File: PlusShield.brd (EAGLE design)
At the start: 79.7 x 67.3 mm, 32 parts, among them K1 G6J-2P-Y, K2 G6J-2P-Y

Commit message: Added PNGs and gnd vias.
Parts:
- added U$4, U$5: (no value), Robin:SAFECAST_LOGO
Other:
- board text added: "License CC-BY-SA 3.0"
- board text added: "PlusShield v1.0"
- board text added: "SAFECAST Japan"
- board text added: "by Robin Scheibler and Joe Moross"
- board text added: "https://github.com/Safecast/PlusShield"
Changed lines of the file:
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@@
 <text x="56.642" y="9.652" size="0.762" layer="21" rot="R90">5V</text>
 <text x="56.896" y="5.334" size="0.762" layer="21" rot="R180">PULSE</text>
+<text x="2.54" y="63.5" size="1.778" layer="21">PlusShield v1.0</text>
+<text x="26.67" y="64.77" size="0.762" layer="21">by Robin Scheibler and Joe Moross</text>
+<text x="26.67" y="63.5" size="0.762" layer="21">License CC-BY-SA 3.0</text>
+<text x="26.67" y="62.23" size="0.762" layer="21">https://github.com/Safecast/PlusShield</text>
+<text x="2.54" y="60.96" size="1.778" layer="21">SAFECAST Japan</text>
 </plain>
 <attributes>
@@
 <element name="C2" library="SparkFun" package="CAP-PTH-5MM" value="0.1uF" x="70.5358" y="54.0512" rot="R90"/>
 <element name="USB2" library="SparkFun" package="1X04" value="" x="77.47" y="11.43" smashed="yes" rot="R90">
-<attribute name="NAME" x="77.9272" y="21.0058" size="1.27" layer="25" ratio="10" rot="R90"/>
 <attribute name="VALUE" x="80.645" y="10.16" size="1.27" layer="27" rot="R90"/>
 </element>
 <element name="USB1" library="SparkFun" package="1X04" value="" x="64.77" y="2.54" smashed="yes" rot="R90">
-<attribute name="NAME" x="65.2272" y="12.1158" size="1.27" layer="25" ratio="10" rot="R90"/>
 <attribute name="VALUE" x="67.945" y="1.27" size="1.27" layer="27" rot="R90"/>
 </element>
@@
 </element>
 <element name="SIG1" library="SparkFun" package="1X04" value="" x="58.42" y="2.54" smashed="yes" rot="R90">
-<attribute name="NAME" x="58.8772" y="12.1158" size="1.27" layer="25" ratio="10" rot="R90"/>
 <attribute name="VALUE" x="61.595" y="1.27" size="1.27" layer="27" rot="R90"/>
 </element>
@@
 </element>
 <element name="PWR1" library="SparkFun" package="1X05" value="" x="64.77" y="54.61" smashed="yes" rot="R90">
-<attribute name="NAME" x="65.4812" y="48.6918" size="1.27" layer="25" ratio="10" rot="R90"/>
 <attribute name="VALUE" x="67.945" y="53.34" size="1.27" layer="27" rot="R90"/>
 </element>
-<element name="R10" library="adafruit" package="0207/10" value="10K" x="20.32" y="46.99" rot="R90"/>
-<element name="R11" library="adafruit" package="0207/10" value="1K" x="17.78" y="46.99" rot="R90"/>
-<element name="R12" library="adafruit" package="0207/10" value="10K" x="13.97" y="46.99" rot="R90"/>
-<element name="R13" library="adafruit" package="0207/10" value="1K" x="11.43" y="46.99" rot="R90"/>
+<element name="R10" library="adafruit" package="0207/10" value="10K" x="20.32" y="46.99" smashed="yes" rot="R90">
+<attribute name="NAME" x="21.082" y="45.212" size="1.27" layer="25" ratio="10" rot="R90"/>
+</element>
+<element name="R11" library="adafruit" package="0207/10" value="1K" x="17.78" y="46.99" smashed="yes" rot="R90">
+<attribute name="NAME" x="18.542" y="45.212" size="1.27" layer="25" ratio="10" rot="R90"/>
+</element>
+<element name="R12" library="adafruit" package="0207/10" value="10K" x="13.97" y="46.99" smashed="yes" rot="R90">
+<attribute name="NAME" x="14.732" y="45.212" size="1.27" layer="25" ratio="10" rot="R90"/>
+</element>
+<element name="R13" library="adafruit" package="0207/10" value="1K" x="11.43" y="46.99" smashed="yes" rot="R90">
+<attribute name="NAME" x="12.192" y="45.212" size="1.27" layer="25" ratio="10" rot="R90"/>
+</element>
 <element name="JP1" library="SparkFun" package="1X10" value="M10&quot;" x="2.54" y="15.24" smashed="yes" rot="R90"/>
 <element name="JP2" library="SparkFun" package="1X10" value="M10&quot;" x="5.08" y="15.24" smashed="yes" rot="R90"/>
@@
 <element name="JP5" library="SparkFun" package="1X10" value="M10&quot;" x="12.7" y="15.24" smashed="yes" rot="R90"/>
 <element name="JP6" library="SparkFun" package="1X10" value="M10&quot;" x="15.24" y="15.24" smashed="yes" rot="R90"/>
+<element name="U$4" library="Robin" package="SAFECAST_LOGO" value="" x="53.34" y="24.13" rot="MR90"/>
+<element name="U$5" library="Robin" package="SAFECAST_LOGO" value="" x="45.72" y="48.26"/>
 </elements>
 <signals>
@@
 <vertex x="-5.6134" y="68.7324"/>
 </polygon>
+<via x="2.54" y="58.42" extent="1-16" drill="0.4064"/>
+<via x="5.08" y="58.42" extent="1-16" drill="0.4064"/>
+<via x="5.08" y="55.88" extent="1-16" drill="0.4064"/>
+<via x="2.54" y="55.88" extent="1-16" drill="0.4064"/>
+<via x="2.54" y="53.34" extent="1-16" drill="0.4064"/>
+<via x="5.08" y="53.34" extent="1-16" drill="0.4064"/>
+<via x="7.62" y="53.34" extent="1-16" drill="0.4064"/>
+<via x="7.62" y="55.88" extent="1-16" drill="0.4064"/>
+<via x="7.62" y="58.42" extent="1-16" drill="0.4064"/>
 </signal>
 <signal name="N$7">
@@
 <wire x1="20.3708" y1="58.3692" x2="20.32" y2="58.42" width="0.4064" layer="1"/>
 </signal>
+<signal name="GND1">
+<via x="2.54" y="49.53" extent="1-16" drill="0.4064"/>
+<via x="5.08" y="49.53" extent="1-16" drill="0.4064"/>
+<via x="5.08" y="46.99" extent="1-16" drill="0.4064"/>
+<via x="2.54" y="46.99" extent="1-16" drill="0.4064"/>
+<via x="2.54" y="44.45" extent="1-16" drill="0.4064"/>
+<via x="5.08" y="44.45" extent="1-16" drill="0.4064"/>
+<via x="7.62" y="44.45" extent="1-16" drill="0.4064"/>
+<via x="7.62" y="46.99" extent="1-16" drill="0.4064"/>
+<via x="7.62" y="49.53" extent="1-16" drill="0.4064"/>
+</signal>
+<signal name="GND2">
+<via x="2.54" y="7.62" extent="1-16" drill="0.4064"/>
+<via x="5.08" y="7.62" extent="1-16" drill="0.4064"/>
+<via x="5.08" y="5.08" extent="1-16" drill="0.4064"/>
+<via x="2.54" y="5.08" extent="1-16" drill="0.4064"/>
+<via x="2.54" y="2.54" extent="1-16" drill="0.4064"/>
+<via x="5.08" y="2.54" extent="1-16" drill="0.4064"/>
+<via x="7.62" y="2.54" extent="1-16" drill="0.4064"/>
+<via x="7.62" y="5.08" extent="1-16" drill="0.4064"/>
+<via x="7.62" y="7.62" extent="1-16" drill="0.4064"/>
+</signal>
+<signal name="GND3">
+<via x="17.78" y="5.08" extent="1-16" drill="0.4064"/>
+<via x="15.24" y="5.08" extent="1-16" drill="0.4064"/>
+<via x="15.24" y="2.54" extent="1-16" drill="0.4064"/>
+<via x="17.78" y="2.54" extent="1-16" drill="0.4064"/>
+<via x="20.32" y="2.54" extent="1-16" drill="0.4064"/>
+<via x="20.32" y="5.08" extent="1-16" drill="0.4064"/>
+</signal>
+<signal name="GND4">
+<via x="50.8" y="15.24" extent="1-16" drill="0.4064"/>
+<via x="48.26" y="15.24" extent="1-16" drill="0.4064"/>
+<via x="53.34" y="15.24" extent="1-16" drill="0.4064"/>
+<via x="22.86" y="16.51" extent="1-16" drill="0.4064"/>
+<via x="22.86" y="19.05" extent="1-16" drill="0.4064"/>
+<via x="22.86" y="21.59" extent="1-16" drill="0.4064"/>
+<via x="22.86" y="21.59" extent="1-16" drill="0.4064"/>
+<via x="29.21" y="29.21" extent="1-16" drill="0.4064"/>
+<via x="22.86" y="31.75" extent="1-16" drill="0.4064"/>
+<via x="68.58" y="16.51" extent="1-16" drill="0.4064"/>
+<via x="25.4" y="34.29" extent="1-16" drill="0.4064"/>
+<via x="26.67" y="39.37" extent="1-16" drill="0.4064"/>
+<via x="62.23" y="24.13" extent="1-16" drill="0.4064"/>
+<via x="62.23" y="27.94" extent="1-16" drill="0.4064"/>
+<via x="62.23" y="31.75" extent="1-16" drill="0.4064"/>
+<via x="62.23" y="39.37" extent="1-16" drill="0.4064"/>
+<via x="71.12" y="24.13" extent="1-16" drill="0.4064"/>
+<via x="71.12" y="27.94" extent="1-16" drill="0.4064"/>
+<via x="71.12" y="31.75" extent="1-16" drill="0.4064"/>
+<via x="71.12" y="35.56" extent="1-16" drill="0.4064"/>
+<via x="71.12" y="39.37" extent="1-16" drill="0.4064"/>
+<via x="62.23" y="43.18" extent="1-16" drill="0.4064"/>
+<via x="71.12" y="43.18" extent="1-16" drill="0.4064"/>
+<via x="49.53" y="54.61" extent="1-16" drill="0.4064"/>
+<via x="60.96" y="54.61" extent="1-16" drill="0.4064"/>
+<via x="46.99" y="58.42" extent="1-16" drill="0.4064"/>
+<via x="40.64" y="60.96" extent="1-16" drill="0.4064"/>
+<via x="33.02" y="49.53" extent="1-16" drill="0.4064"/>
+<via x="29.21" y="53.34" extent="1-16" drill="0.4064"/>
+<via x="15.24" y="46.99" extent="1-16" drill="0.4064"/>
+<via x="71.12" y="11.43" extent="1-16" drill="0.4064"/>
+<via x="53.34" y="2.54" extent="1-16" drill="0.4064"/>
+<via x="49.53" y="2.54" extent="1-16" drill="0.4064"/>
+<via x="45.72" y="2.54" extent="1-16" drill="0.4064"/>
+<via x="46.99" y="46.99" extent="1-16" drill="0.4064"/>
+</signal>
 </signals>

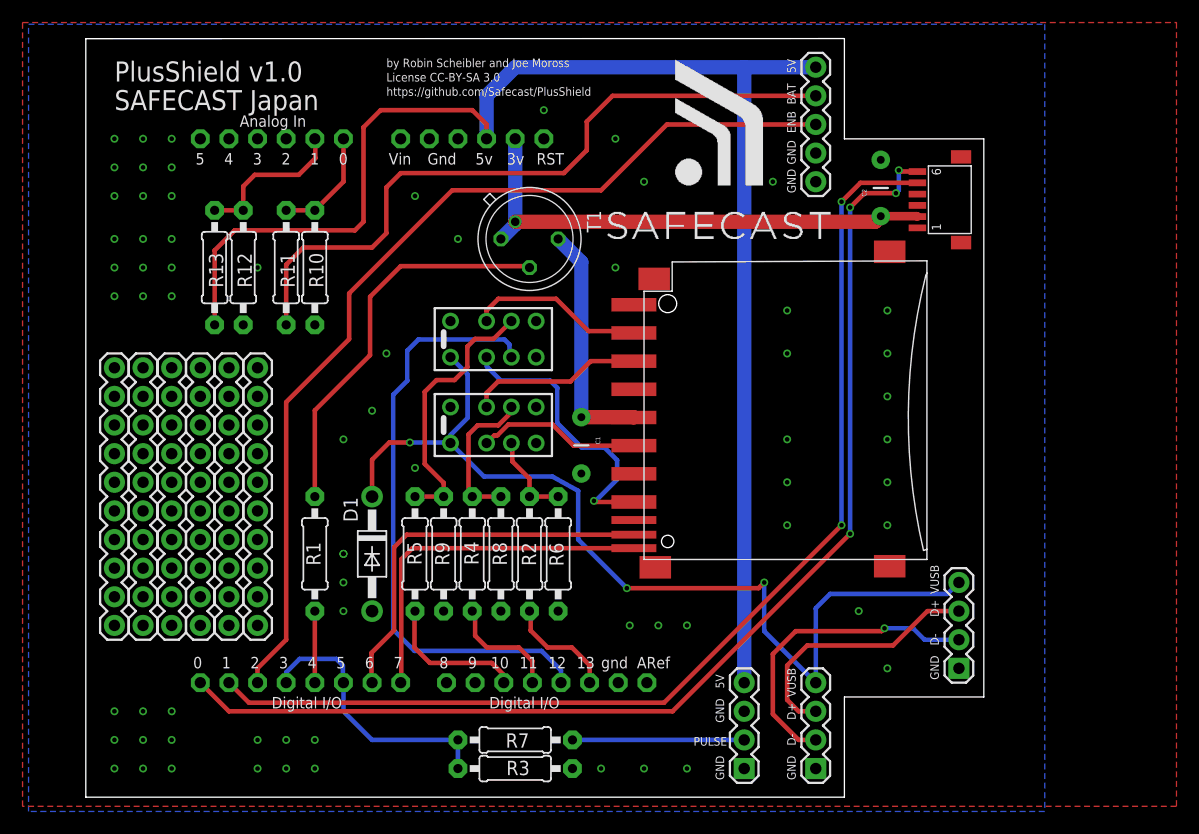
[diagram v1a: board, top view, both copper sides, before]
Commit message: Added bigger proto area. Extra holes for arduino pins.
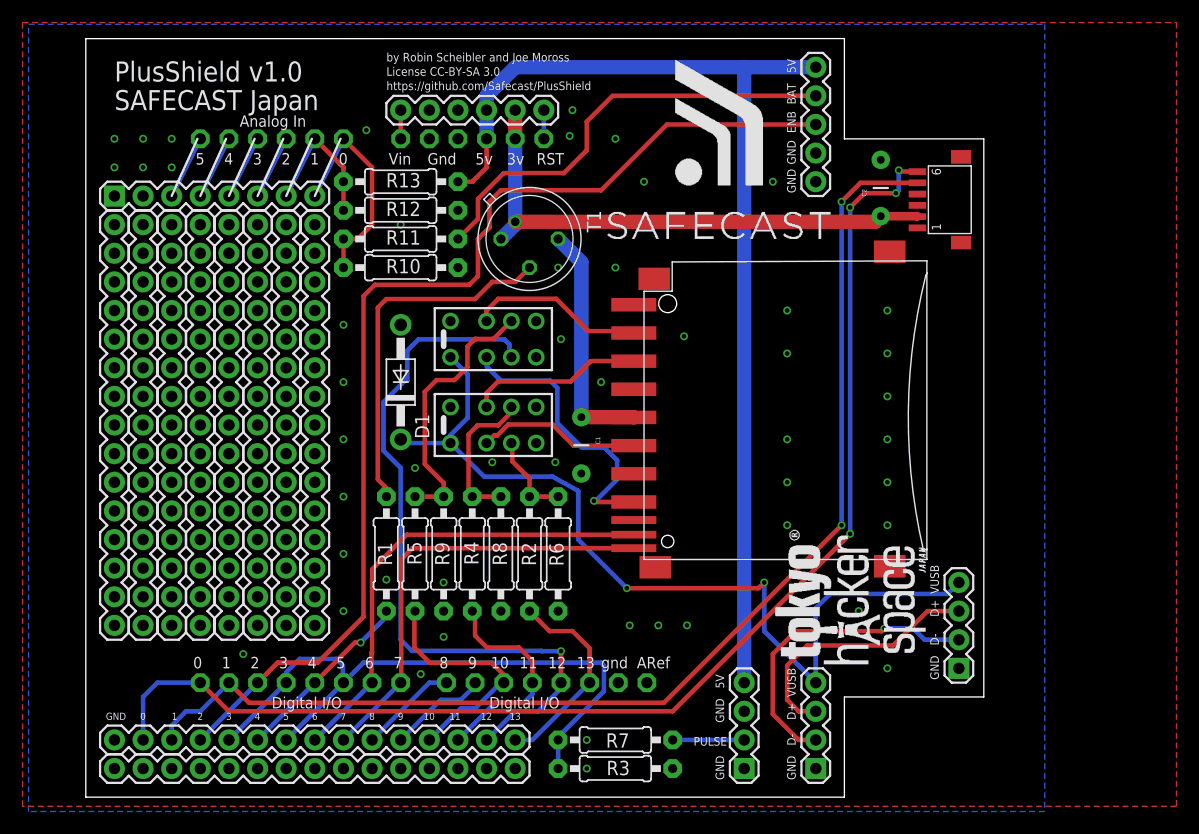
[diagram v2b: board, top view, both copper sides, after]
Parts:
- added JP10, JP11, JP7, JP8: M15, SparkFun:1X15
- added JP12: (no value), SparkFun:1X06
- added JP9: (no value), SparkFun:1X08
- added U$6: (no value), tayken:THS
- JP1, JP2, JP3, JP4, JP5, JP6: value M10" -> M15; device SparkFun:1X10 -> SparkFun:1X15
- moved R13 18.2 mm to (27.9, 54.6), turned to 180 degrees
- moved D1 15.5 mm to (27.9, 36.8), turned to 90 degrees
- moved R12 14.9 mm to (27.9, 52.1), turned to 180 degrees
- moved R11 10.5 mm to (27.9, 49.5), turned to 180 degrees
- moved R3 8.89 mm to (47.0, 2.54)
- moved R7 8.89 mm to (47.0, 5.08)
- moved R10 7.62 mm to (27.9, 47.0), turned to 180 degrees
- moved R1 6.35 mm to (26.7, 21.6)
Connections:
- removed net VIN: U$2.VIN
- new net N$18: JP10.10, U$2.D8
- new net N$19: JP12.1, U$2.VIN
- new net N$20: JP12.6, U$2.RESET
- new net N$21: JP9.3, U$2.A5
- new net N$22: JP9.4, U$2.A4
- new net N$23: JP9.5, U$2.A3
- new net N$24: JP9.6, U$2.A2
- new net N$4: JP10.11, U$2.D9
- net BATT_SENSE: now also JP9.8
- net CDET: now also JP10.8
- net ENBL: now also JP10.4
- net GND: now also JP10.1, JP12.2, JP12.3
- net N$1: now also JP10.6
- net N$12: now also JP10.14
- net N$15: now also JP10.2
- net N$16: now also JP10.3
- net N$3: now also JP10.15
- net N$5: now also JP10.13
- net N$6: now also JP10.12
- net PULSE: now also JP10.5, JP10.7
- net VCC3: now also JP12.5
- net VCC5: now also JP12.4
- net VCC5_SENSE: now also JP9.7
- net WPROT: now also JP10.9
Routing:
- net VCC5: track 131.3 -> 94.3 mm
- net PULSE: track 24.5 -> 57.4 mm
- net VBATT: track 62.4 -> 39.5 mm
- net ENBL: track 85.5 -> 97.2 mm
- net N$12: track 53.6 -> 64.6 mm, vias 0 -> 1
- net N$1: track 6.35 -> 16.5 mm, vias 0 -> 1
- net BATT_SENSE: track 9.94 -> 20.0 mm
- net N$15: track 102.6 -> 112.0 mm
- net N$5: track 10.2 -> 19.5 mm
- net N$17: track 15.2 -> 6.35 mm
- net N$4: track 0.00 -> 8.86 mm
- net N$6: track 12.9 -> 21.6 mm
- net N$18: track 0.00 -> 8.71 mm
- net N$3: track 9.82 -> 18.5 mm
- net N$16: track 97.7 -> 105.7 mm
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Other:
- board text added: "0"
- board text added: "1"
- board text added: "10"
- board text added: "11"
- board text added: "12"
- board text added: "13"
- board text added: "2"
- board text added: "3"
- board text added: "4"
- board text added: "5"
- board text added: "6"
- board text added: "7"
- board text added: "8"
- board text added: "9"

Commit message: Moved USB connector to other side. Added some labels on silkscreen. Put strain relief holes for Inspector connection. Moved board boundary. Added breakout USB connector dongle.
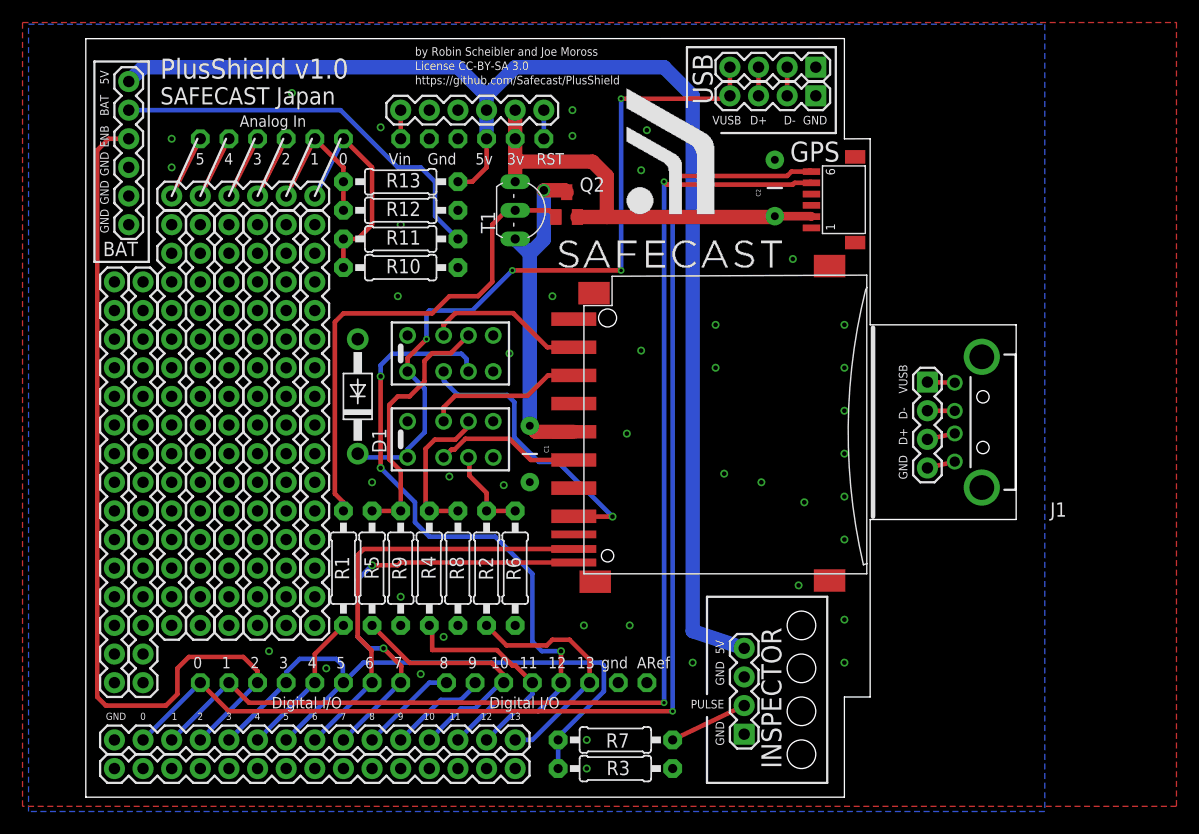
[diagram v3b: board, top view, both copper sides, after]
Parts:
- removed PWR1: (no value), SparkFun:1X05
- added J1: (no value), SeeedConnector:A-DIP
- added JP13: (no value), SparkFun:1X06
- added Q2: SMD, transistor-pnp:SOT23
- added U$7: (no value), SeeedLogo:OSHW_FILLX350_NOTEXT
- added USB3: (no value), SparkFun:1X04
- JP9: device SparkFun:1X08 -> SparkFun:1X06
- R10, R12: value 10K -> 1K
- R11, R13: value 1K -> 9.1K
- T1: value (none) -> TH; device transistor:TO5 -> transistor-pnp:TO92-CBE
- moved USB1 59.7 mm to (64.8, 62.2), turned to 180 degrees
- moved USB2 54.8 mm to (64.8, 64.8), turned to 180 degrees
- moved U$6 31.7 mm to (46.0, 11.2), flipped to the bottom
- moved U$4 15.5 mm to (46.2, 37.8)
- moved U$3 9.40 mm to (69.2, 56.2)
- moved C2 9.40 mm to (61.1, 54.1)
- moved U$1 5.48 mm to (44.2, 33.0)
- moved JP1 5.08 mm to (2.54, 10.2)
- moved JP2 5.08 mm to (5.08, 10.2)
- moved JP9 5.08 mm to (7.62, 53.3)
- moved U$5 5.01 mm to (41.4, 45.7)
- moved C1 4.64 mm to (39.4, 30.5)
- moved K1 4.02 mm to (31.8, 39.4)
- moved K2 4.02 mm to (31.8, 31.8)
- moved R1 4.02 mm to (22.9, 20.3)
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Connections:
- new net D+_C: J1.D+, USB3.3
- new net D-_C: J1.D-, USB3.2
- new net GND_C: J1.GND, USB3.4
- new net VBUS_C: J1.VBUS, USB3.1
- net BATT_SENSE: now also JP9.6; no longer JP9.8
- net ENBL: now also JP13.4; no longer PWR1.3
- net GND: now also JP13.2, JP13.3; no longer PWR1.1, PWR1.2
- net N$2: now also Q2.1, T1.B; no longer T1.2
- net N$21: now also JP9.1; no longer JP9.3
- net N$22: now also JP9.2; no longer JP9.4
- net N$23: now also JP9.3; no longer JP9.5
- net N$24: now also JP9.4; no longer JP9.6
- net VBATT: now also JP13.5; no longer PWR1.4
- net VCC3: now also Q2.2, T1.E; no longer T1.1
- net VCC5: now also JP13.6; no longer PWR1.5
- net VCC5_SENSE: now also JP9.5; no longer JP9.7
- net VDD: now also Q2.3, T1.C; no longer T1.3
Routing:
- net D-: track 28.2 -> 2.54 mm, vias 1 -> 0
- net VCC5: track 94.3 -> 115.5 mm
- net D+: track 23.2 -> 2.54 mm
- net ENBL: track 97.2 -> 78.1 mm
- net VBUS: track 80.2 -> 65.7 mm, vias 2 -> 4
- net N$2: track 32.0 -> 44.0 mm
- net VCC3: track 47.9 -> 39.5 mm, vias 1 -> 0
- net VDD: track 21.3 -> 29.5 mm, vias 0 -> 1
- net N$12: track 64.6 -> 57.6 mm, vias 1 -> 3
- net VBATT: track 39.5 -> 35.7 mm
- net CDET: track 41.8 -> 38.4 mm
- net N$3: track 18.5 -> 21.6 mm
- net N$1: track 16.5 -> 13.8 mm, vias 1 -> 0
- net GND_C: track 0.00 -> 2.49 mm
- net D+_C: track 0.00 -> 2.48 mm
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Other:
- board size 79.7 x 67.3 mm -> 82.5 x 67.3 mm
- board text added: "GPS"
- board text added: "INSPECTOR"
- board text added: "USB"
